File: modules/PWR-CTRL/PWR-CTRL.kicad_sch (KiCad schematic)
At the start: 12 parts, among them SW1 POWER ON, SW2 RESET

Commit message: added joshua
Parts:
- added C1: 47µF, Capacitor_THT:CP_Radial_D5.0mm_P2.50mm, symbol IMNOTWOPR:C_Polarized
- added C2: 100n, IMNOTWOPR:C_Rect_P200mil, symbol IMNOTWOPR:C
- added U1: 74HC00, IMNOTWOPR:DIP-14N, symbol 74xx:74HC00
- renumbered C1 to C3
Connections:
- net +5VSB: now also C1.1, C2.1, U1.10, U1.14 (VCC); no longer R1.2
- net GND: now also C1.2, C2.2, U1.12, U1.13, U1.4, U1.5, U1.7 (GND)
- net PWROK: now also U1.1, U1.2
- net at R1.1: now also U1.8; no longer D1.2 (A)
- new net: U1.3, U1.9
- new net: D1.2 (A), R1.2
- no-connect marks 1 -> 3
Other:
- moved on the sheet: D1, R1

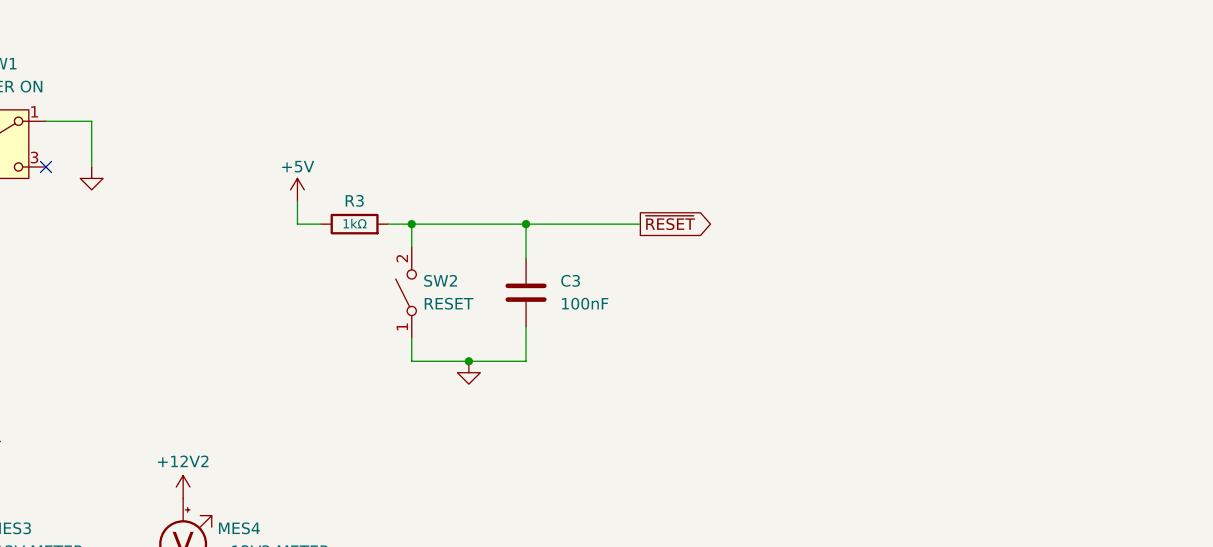
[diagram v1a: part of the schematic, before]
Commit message: added i2c pullups to pwr-ctrl
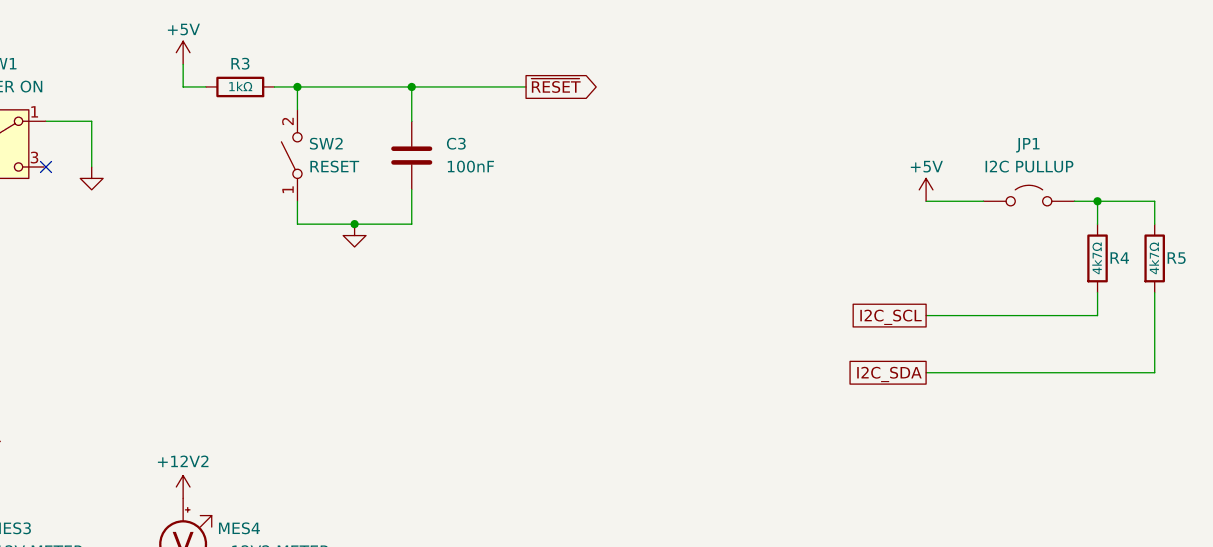
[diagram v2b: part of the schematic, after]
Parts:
- added JP1: I2C PULLUP, FormantKO:Jumper_1x02, symbol Jumper:Jumper_2_Open
- added R4, R5: 4k7Ω, IMNOTWOPR:R_Axial_DIN0207_P400mil, symbol IMNOTWOPR:R
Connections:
- net +5V: now also JP1.1 (A)
- new net: JP1.2 (B), R4.1, R5.1
- new net I2C_SCL: R4.2
- new net I2C_SDA: R5.2
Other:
- moved on the sheet: C3, R3, SW2
